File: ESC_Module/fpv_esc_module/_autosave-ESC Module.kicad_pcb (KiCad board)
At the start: 4 copper layers, 16 x 26.2 mm, 127 parts, among them U204 STM32F051K8, U25 FD6288Q, U301 STM32F051K8, U302 FD6288Q

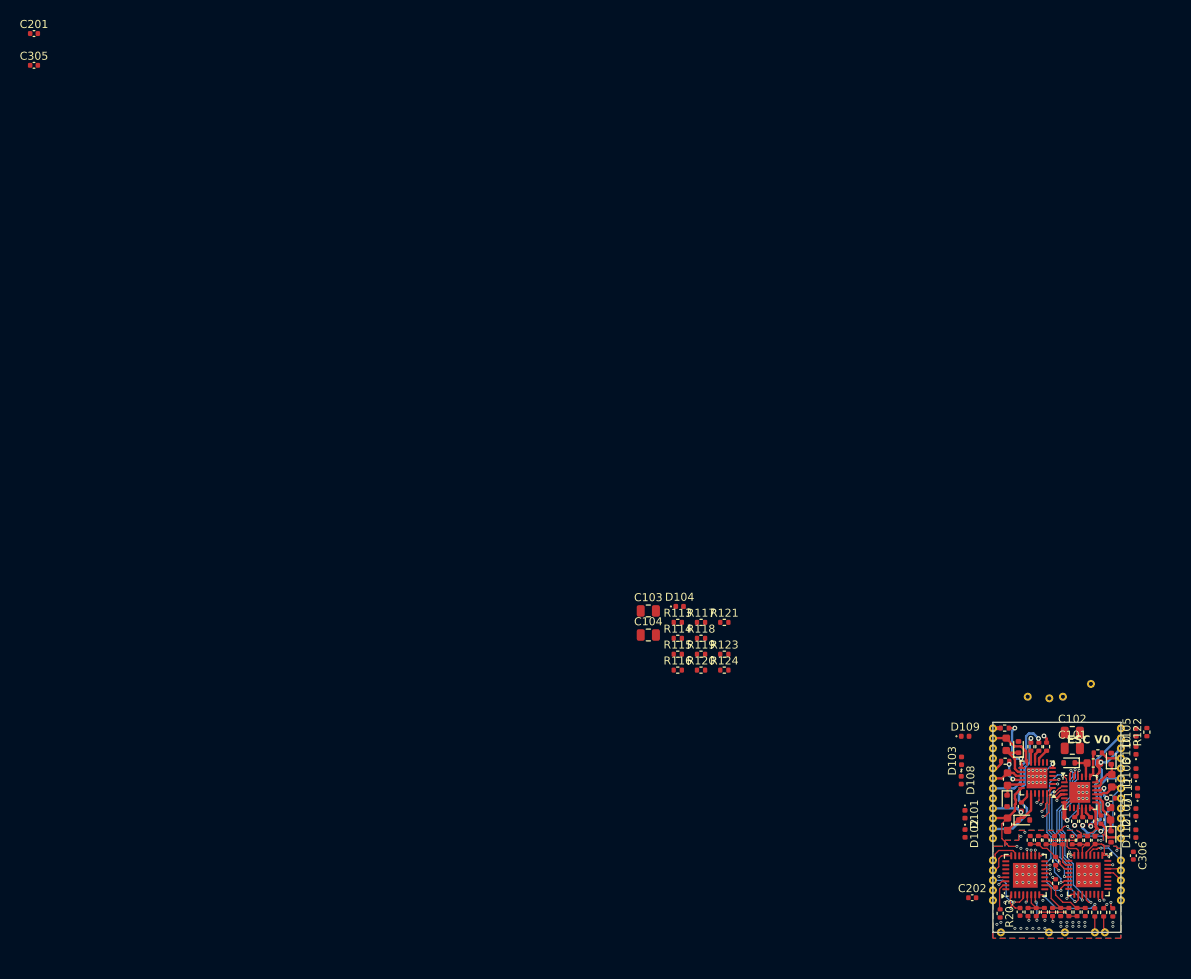
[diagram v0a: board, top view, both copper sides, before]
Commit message: Schematic changes made
Made changes to the schematic just starting routing
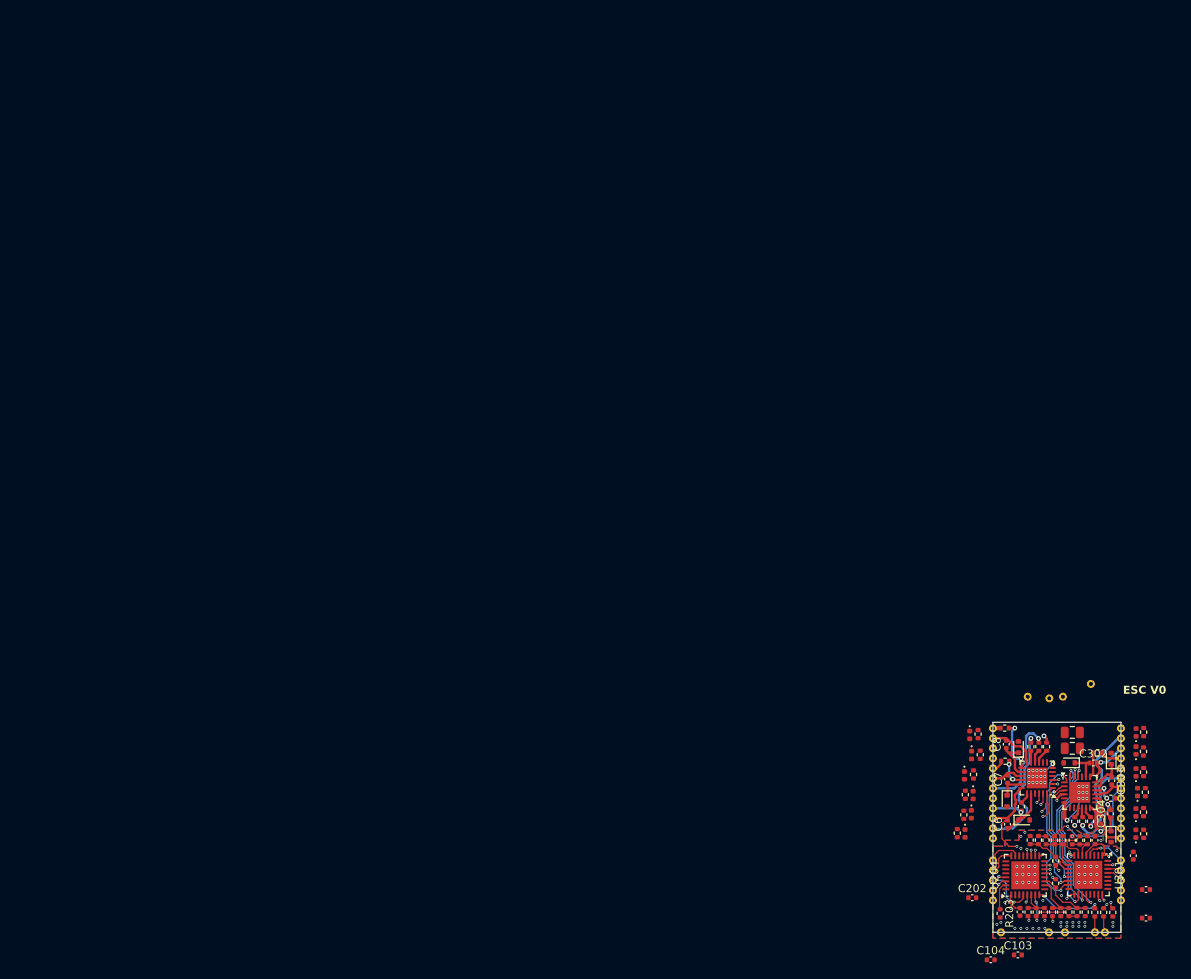
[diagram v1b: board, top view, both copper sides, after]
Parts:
- C103, C104: value 22uF -> 10uF; footprint Capacitor_SMD:C_0805_2012Metric -> Capacitor_SMD:C_0402_1005Metric
- C302, C303, C304, C6, C7, C8: footprint Capacitor_SMD:C_0603_1608Metric -> Capacitor_SMD:C_0402_1005Metric
- U204, U301: footprint Package_DFN_QFN:QFN-32-1EP_5x5mm_P0.5mm_EP3.1x3.1mm -> Package_DFN_QFN:UFQFPN-32-1EP_5x5mm_P0.5mm_EP3.5x3.5mm
- moved C201 175.4 mm to (139.1, 101.7)
- moved C305 175.2 mm to (139.1, 105.2)
- moved C103 63.1 mm to (123.1, 109.8)
- moved R118 60.5 mm to (138.8, 94.7), turned to 90 degrees
- moved R117 59.5 mm to (139.1, 89.5), turned to 90 degrees
- moved R116 59.1 mm to (138.8, 84.4), turned to 90 degrees
- moved C104 59.0 mm to (119.7, 110.4)
- moved R124 55.3 mm to (138.8, 92.0), turned to 90 degrees
- moved R123 54.4 mm to (138.8, 87.0), turned to 90 degrees
- moved R113 43.8 mm to (115.5, 94.6), turned to -90 degrees
- moved D104 41.0 mm to (117.3, 84.8), turned to -90 degrees
- moved R114 40.9 mm to (116.6, 89.8), turned to -90 degrees
- moved R115 39.8 mm to (118.4, 84.8), turned to -90 degrees
- moved R119 38.5 mm to (116.4, 92.3), turned to -90 degrees
- moved R120 36.5 mm to (117.6, 87.3), turned to -90 degrees
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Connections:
- R101 pad 1: /ESC1/LO3 -> /ESC1/LO1
- R101 pad 2: Net-(D104-K) -> Net-(D102-K)
- R103 pad 1: /ESC1/LO2 -> /ESC1/HO1
- R103 pad 2: Net-(D103-K) -> Net-(D101-K)
- R104 pad 1: /ESC1/LO1 -> /ESC1/LO2
- R104 pad 2: Net-(D102-K) -> Net-(D103-K)
- R105 pad 1: /ESC1/HO1 -> /ESC1/HO3
- R105 pad 2: Net-(D101-K) -> Net-(D109-K)
- R106 pad 1: /ESC1/HO3 -> /ESC1/LO3
- R106 pad 2: Net-(D109-K) -> Net-(D104-K)
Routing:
- net (no net): track 32.4 -> 0.00 mm, vias 3 -> 0
- net GND: track 104.6 -> 84.9 mm
- net Net-(D102-K): track 0.00 -> 16.0 mm, vias 0 -> 1
- net Net-(D103-K): track 0.00 -> 12.3 mm, vias 0 -> 1
- net Net-(D101-K): track 0.00 -> 3.59 mm, vias 0 -> 1
- net Net-(D109-K): track 0.00 -> 0.53 mm
